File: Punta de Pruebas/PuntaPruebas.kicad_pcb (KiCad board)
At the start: 2 copper layers, 61 x 38.1 mm, 23 parts, among them P1 CONN_2, P2 CONN_1, P3 CONN_1, SW1 Llave Inversora, U1 40106

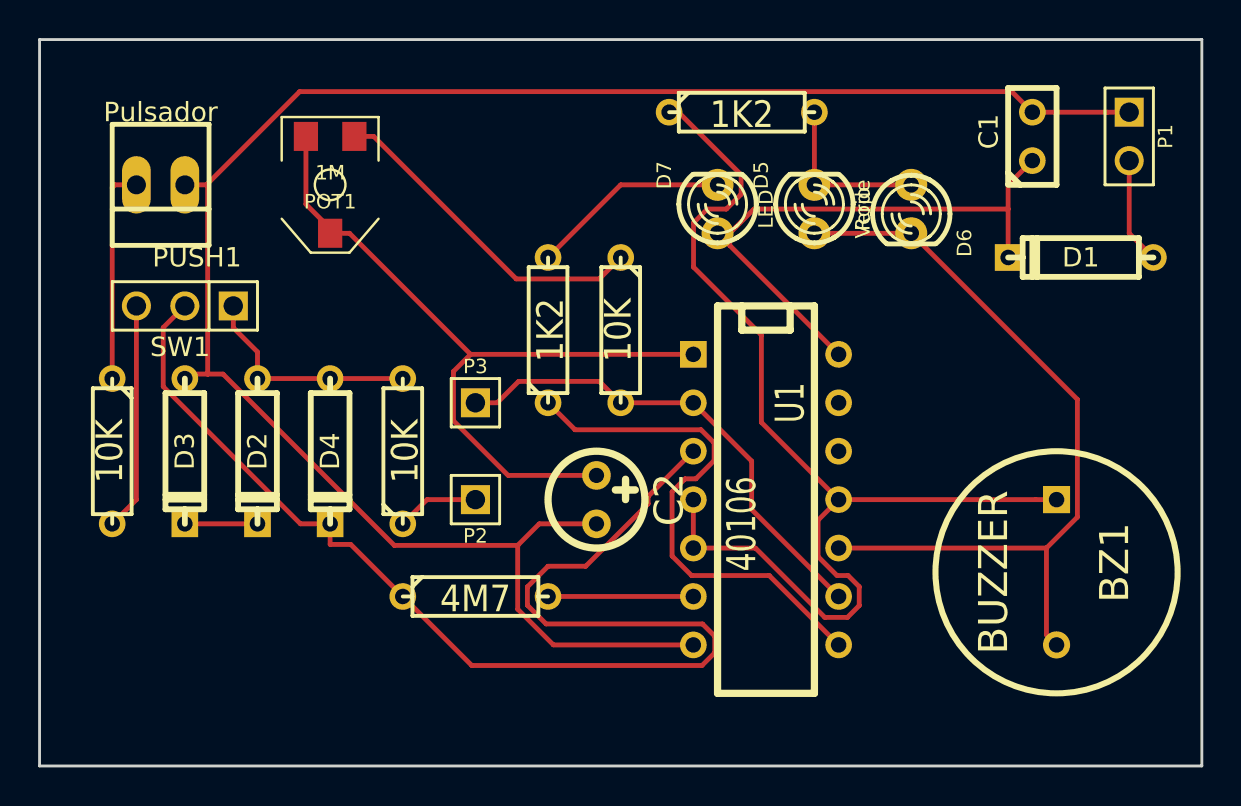
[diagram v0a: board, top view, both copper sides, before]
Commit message: cambio de layout nuevamente, agrando el ancho de las vías para facilitar impresión
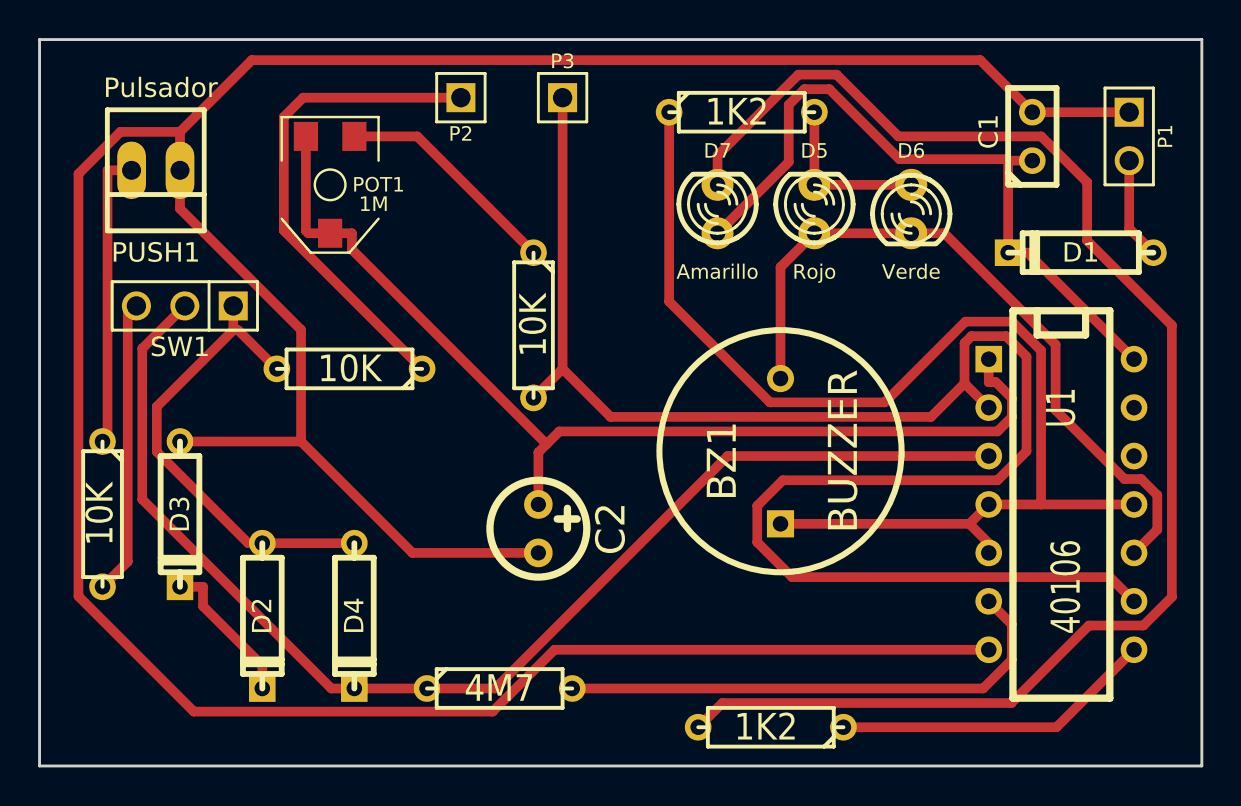
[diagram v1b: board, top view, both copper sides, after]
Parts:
- D7: value LED -> Amarillo
- moved R6 23.9 mm to (211.1, 169.4), turned to 180 degrees
- moved P2 21.1 mm to (194.8, 136.4)
- moved P3 16.6 mm to (200.2, 136.4)
- moved BZ1 15.8 mm to (211.6, 154.9), turned to 90 degrees
- moved U1 15.5 mm to (226.3, 157.7)
- moved D4 8.73 mm to (189.2, 163.6)
- moved D2 8.64 mm to (184.4, 163.6)
- moved R1 5.14 mm to (189.0, 150.6), turned to 180 degrees
- moved R4 4.99 mm to (196.8, 167.4)
- moved R3 4.58 mm to (198.6, 148.3)
- moved C2 3.41 mm to (198.9, 159.0)
- moved R2 3.34 mm to (176.0, 158.2)
- moved D3 3.31 mm to (180.1, 158.2)
- moved PUSH1 0.80 mm to (178.8, 140.2)
- moved D1 0.25 mm to (227.3, 144.5)
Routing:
- net VSS: track 101.2 -> 172.5 mm
- net N-0000017: track 10.5 -> 76.3 mm
- net N-0000012: track 25.7 -> 90.2 mm
- net N-0000016: track 4.34 -> 25.9 mm
- net N-000009: track 7.62 -> 27.2 mm
- net N-0000013: track 39.9 -> 54.8 mm
- net N-000006: track 12.0 -> 24.8 mm
- net N-0000015: track 27.4 -> 16.9 mm
- net VDD: track 30.1 -> 36.8 mm
- net N-0000014: track 17.5 -> 11.9 mm
- net N-000003: track 42.1 -> 37.6 mm
- net N-000002: track 58.6 -> 63.0 mm
- net N-0000011: track 11.4 -> 15.6 mm
- net N-000004: track 3.81 -> 7.83 mm
- net N-0000010: track 12.0 -> 15.5 mm
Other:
- net class Default: trace_width 0.254 -> 0.508
- rule trace_min: 0.254 -> 0.01
- rule via_min_size: 0.889 -> 0.035
